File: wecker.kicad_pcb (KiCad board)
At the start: 2 copper layers, 74 x 56 mm, 29 parts, among them J1 Conn_01x20, J2 Conn_01x05, J3 Conn_01x04, J4 Conn_01x02, Q1 BC818, Q2 BC847, SW1 Hour, SW2 Minute, SW3 Alarm, SW4 Time, SW5 Snooze, U1 MSP430FR4133, Y1 32.768

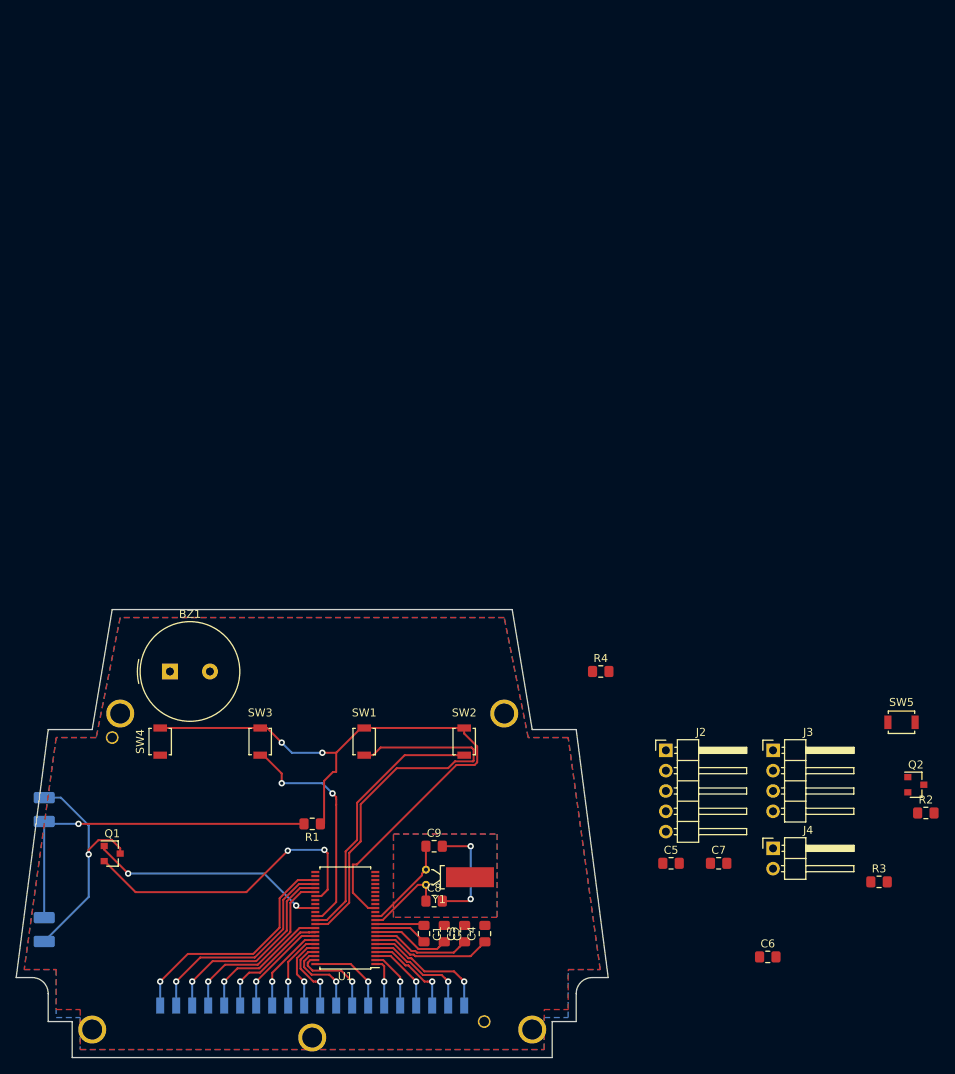
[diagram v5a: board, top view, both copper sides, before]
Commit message: Added TPS61221 Battery Chip
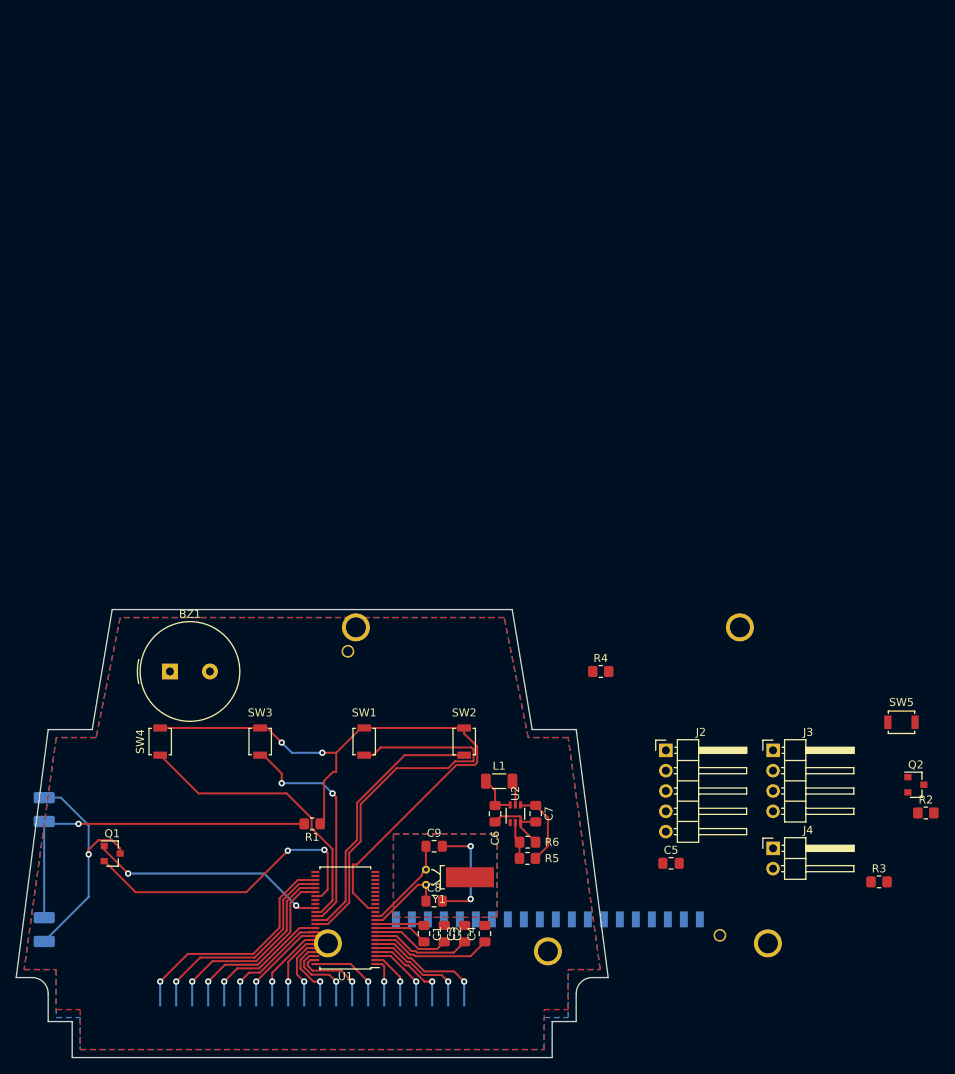
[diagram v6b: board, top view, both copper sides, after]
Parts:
- added L1: 4.7 uH, Inductor_SMD:L_1206_3216Metric_Pad1.22x1.90mm_HandSolder, F.Cu at (123.4, 145.5)
- added R5: R, Resistor_SMD:R_0805_2012Metric_Pad1.20x1.40mm_HandSolder, F.Cu at (126.9, 155.1)
- added R6: R, Resistor_SMD:R_0805_2012Metric_Pad1.20x1.40mm_HandSolder, F.Cu at (126.9, 153.1)
- added U2: TPS61221DCK, Package_TO_SOT_SMD:Texas_R-PDSO-G6, F.Cu at (125.4, 149.5)
- C7: value 100n -> 10u
- Q1: value BC818 -> BC847
- R1: value 1K -> 5K7; footprint Resistor_SMD:R_0805_2012Metric_Pad1.15x1.40mm_HandSolder -> Resistor_SMD:R_0805_2012Metric_Pad1.20x1.40mm_HandSolder
- R2, R3, R4: footprint Resistor_SMD:R_0805_2012Metric_Pad1.15x1.40mm_HandSolder -> Resistor_SMD:R_0805_2012Metric_Pad1.20x1.40mm_HandSolder
- moved C6 38.5 mm to (122.9, 149.5), turned to -90 degrees
- moved J1 31.4 mm to (129.5, 164.2)
- moved C7 23.7 mm to (127.9, 149.5), turned to -90 degrees
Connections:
- C6 pad 1: +BATT -> Net-(C6-Pad1)
- J4 pad 2: +BATT -> Net-(C6-Pad1)
- U1 pad 18: (no net) -> unconnected-(U1-Pad18)
- U1 pad 21: (no net) -> unconnected-(U1-Pad21)
- U1 pad 22: (no net) -> unconnected-(U1-Pad22)
- U1 pad 23: (no net) -> unconnected-(U1-Pad23)
- U1 pad 24: (no net) -> unconnected-(U1-Pad24)
- U1 pad 31: (no net) -> unconnected-(U1-Pad31)
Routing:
- net +BATT: track 83.2 -> 137.2 mm, vias 2 -> 3
- net Net-(D1-Pad2): track 44.2 -> 0.00 mm, vias 1 -> 0
- net unconnected-(U1-Pad31): track 0.00 -> 38.3 mm, vias 0 -> 2
- net Net-(SW4-Pad1): track 0.00 -> 36.3 mm
- net GND: track 38.3 -> 9.36 mm, vias 2 -> 0
- net Net-(C6-Pad1): track 0.00 -> 5.44 mm
- net Net-(R5-Pad2): track 0.00 -> 4.70 mm
- net Net-(L1-Pad2): track 0.00 -> 3.12 mm
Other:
- net class Default removed
